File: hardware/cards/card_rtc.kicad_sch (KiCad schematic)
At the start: 11 parts, among them U1 DS12C887, U2 74HCT138, U3 74HC02, U4 74HCT08, U5 74HCT32, U6 74HCT04

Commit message: Swap DIP sockets to machined-pin versions
V20 DIP-40 -> C2874018, SRAM DIP-32 x2 -> C2874017, DS12C887 DIP-24 ->
C2684765 (all round-hole/machined, verified 600 mil row spacing).
Better grip and repeated-insertion tolerance for the vintage chips;
~$2.50/board-set over stamped tin. Stamped fallbacks noted in
jlcpcb-sourcing.md.

Co-Authored-By: Claude Fable 5 <noreply@anthropic.com>
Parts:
- U1: LCSC Part Num C72120 -> C2684765
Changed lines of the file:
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@@
 			)
 		)
-		(property "LCSC Part Num" "C72120"
+		(property "LCSC Part Num" "C2684765"
 			(at 228.6 116.84 0)
 			(effects

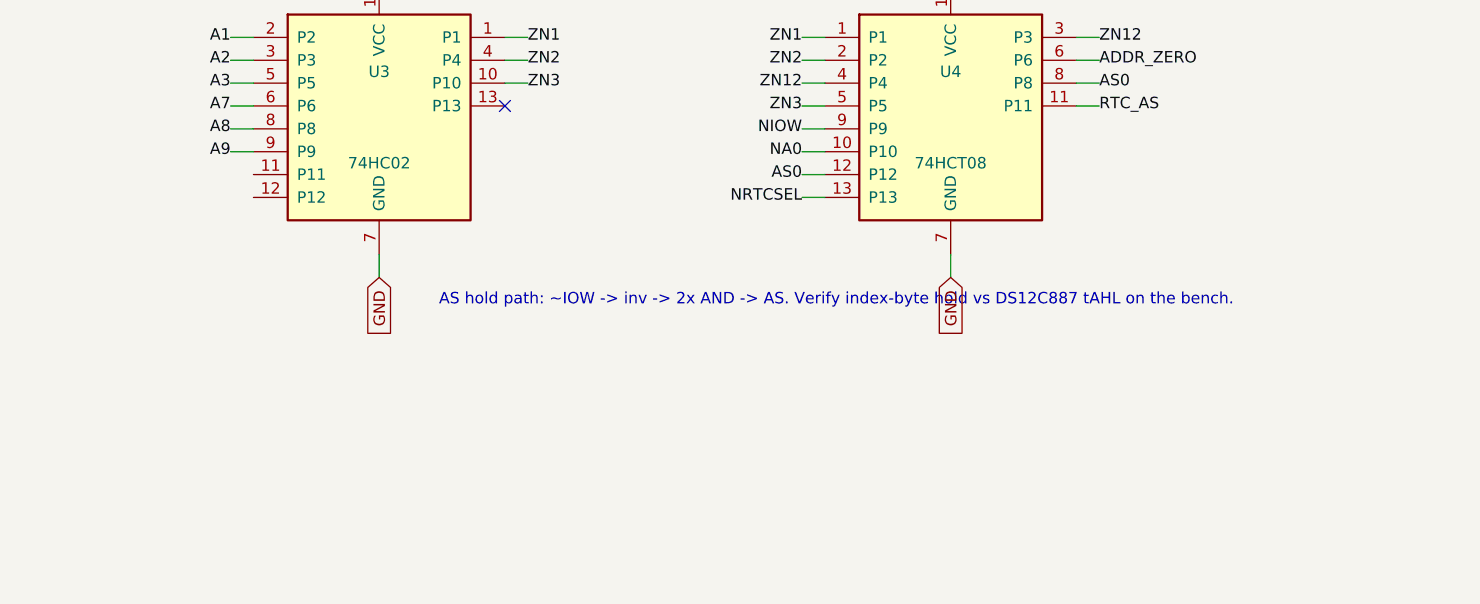
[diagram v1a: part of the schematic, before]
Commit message: Design review 2026-07-11: rail protection, decoupling, wiring fixes
Protection:
- Sidecar +5V now feeds through a 2A polyfuse into +5V_ISA with an
  SMBJ5.0A clamp + 22uF bulk (a faulted ISA card trips its own fuse
  instead of dropping the board; back-fed voltage is clamped).
- USB-C VBUS enters through a 3A polyfuse with an SMBJ5.0A on +5V
  (backstop for the CFG1 9-20V failure mode). CH224K gains a 1uF VDD
  cap; its PG routes to Supervisor GPIO16 as PD_PG. Buck output
  doubled to 2x22uF, 10uF at VIN, extra rail bulk.
- Supervisor USB-A host port: 27R series termination (RP2040
  requirement), USBLC6-2SC6 ESD array, 100uF VBUS bulk.
- Video: HDMI +5V fused (500mA), HPD sensed on GPIO41, 100R series on
  VGA sync. TMDS ESD array deferred to layout (no symbol).
- card_isatest: V5RAW bulk, Q1 gate soft-start cap, TVS on DUT rail.

Wiring fixes:
- SPKR had no driver anywhere (netlist: 1 node). Bus MCU GPIO22
  reassigned from the diagnostics-only bus-CLK sense to SPKR; bus_mcu
  drops CLK from its interface. Doc 5.2 updated.
- bus_mcu C8 decoupled +3V3, a rail that sheet never uses -> 3V3_BUS.
- Storage IRQ5 was push-pull (permanently driven when idle) -> 2N7002
  + gated '125 tri-state, same convention as the LPT IRQ7 stage.
- MAX3241 pump caps resized to the 5V datasheet values (47nF/330nF).
- LPT DB25 status inputs get 4.7k pull-ups (floated with no printer).
- Audio line-out gets a 100R series isolator before the jack.

Best practices:
- Decoupling to ~1x100nF per IC on every sheet + bulk per board
  (cpu_core 7->16 incl. the naked 3.3V oscillator, storage 4->11,
  parallel 6->13, rtc/com/video/bus_mcu/card_isatest similar).
- All floating spare CMOS inputs tied ('00/'74/'157/'02/'04/'125
  sections across cpu_core, bus_mcu, rtc, storage, card_isatest).

Sourcing: new parts mapped in parts.py with JLC-verified LCSC numbers;
Power_Protection lib registered in the tools; TPS563200 stock alert
(4 pcs left at JLC) flagged in parts.py + jlcpcb-sourcing.md. All
decisi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
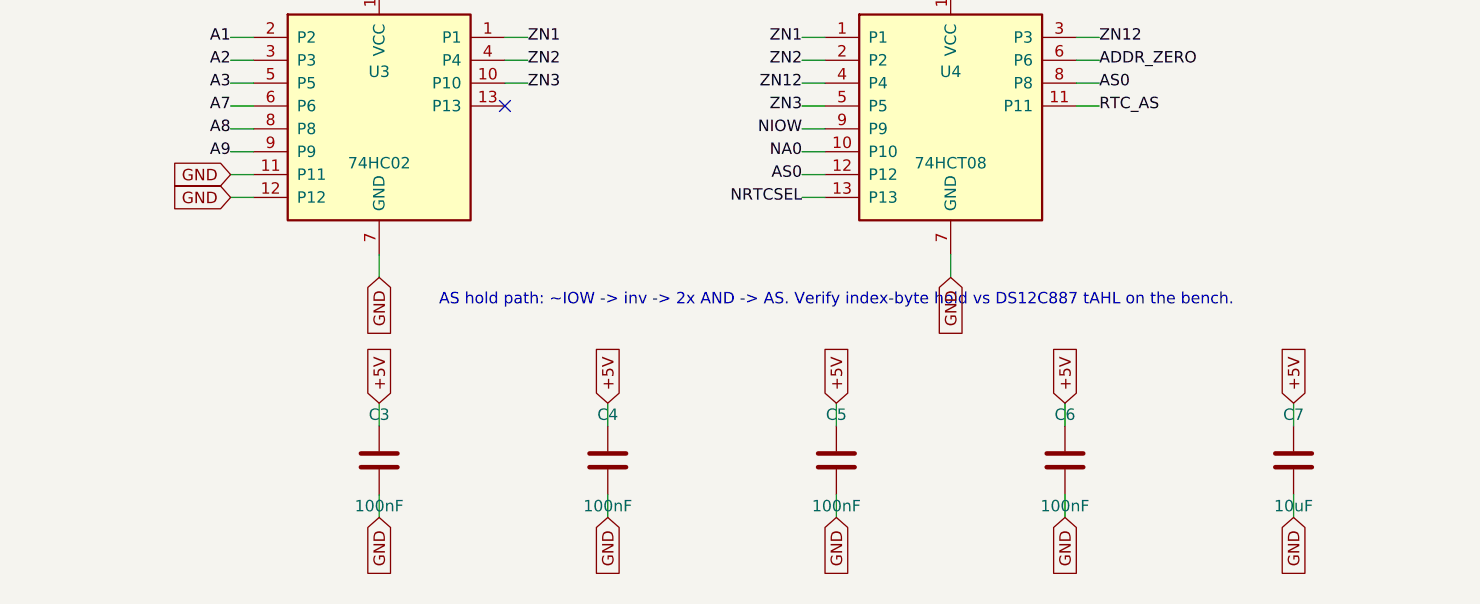
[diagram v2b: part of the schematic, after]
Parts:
- added C3, C4, C5, C6: 100nF, symbol Device:C
- added C7: 10uF, symbol Device:C
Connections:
- net +5V: now also C3.1, C4.1, C5.1, C6.1, C7.1
- net GND: now also U3.11 (P11), U3.12 (P12), C3.2, C4.2, C5.2, C6.2, C7.2
